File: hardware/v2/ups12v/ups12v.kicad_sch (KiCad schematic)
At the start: 0 parts

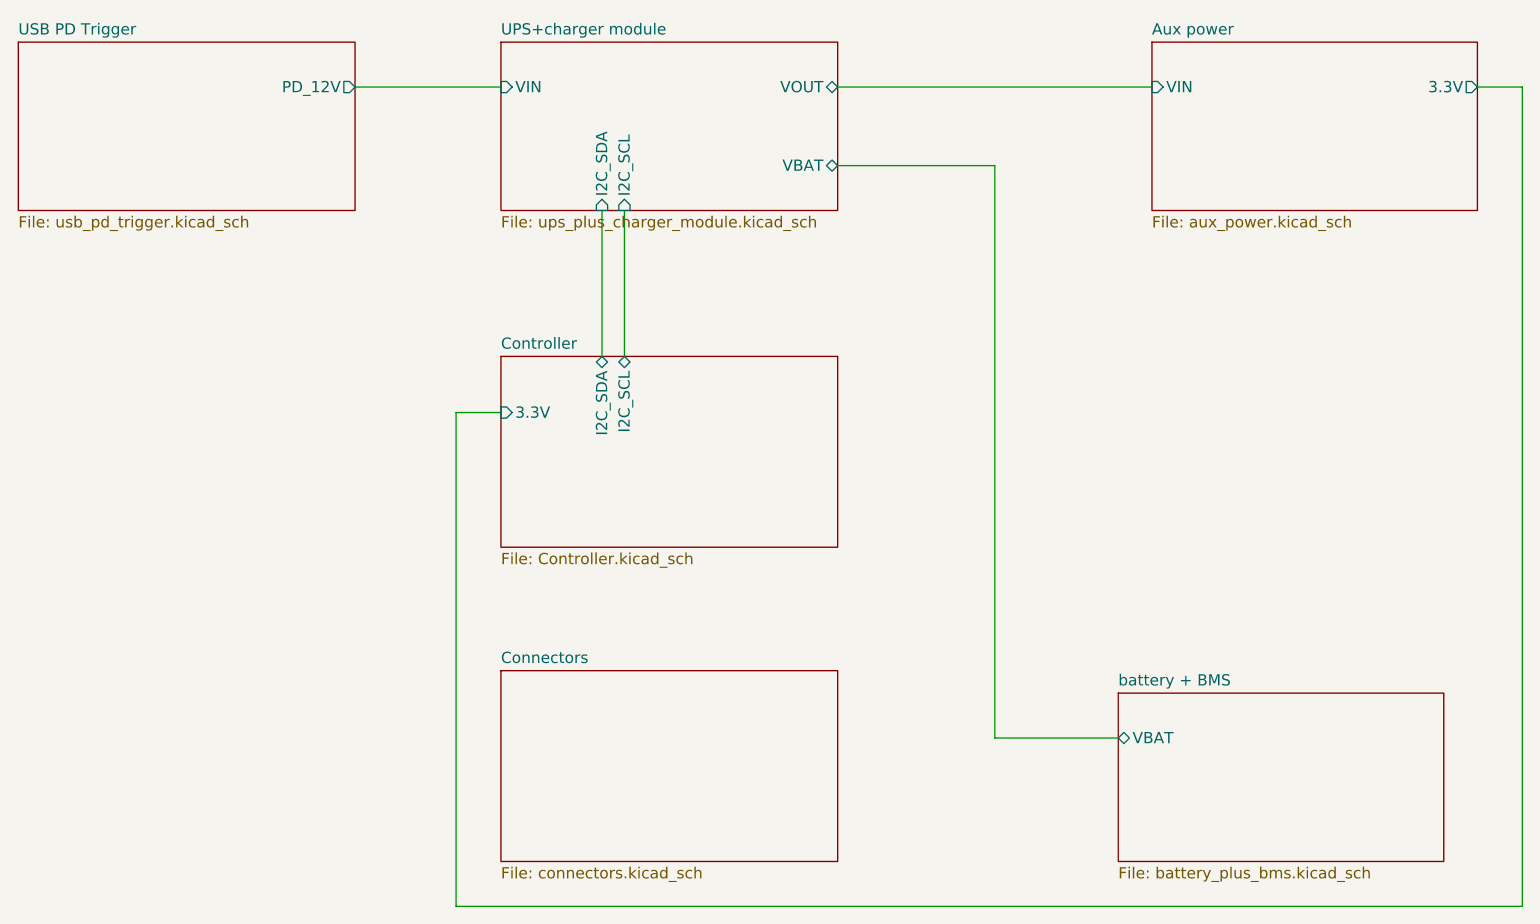
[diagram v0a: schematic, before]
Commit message: add power output to the J4
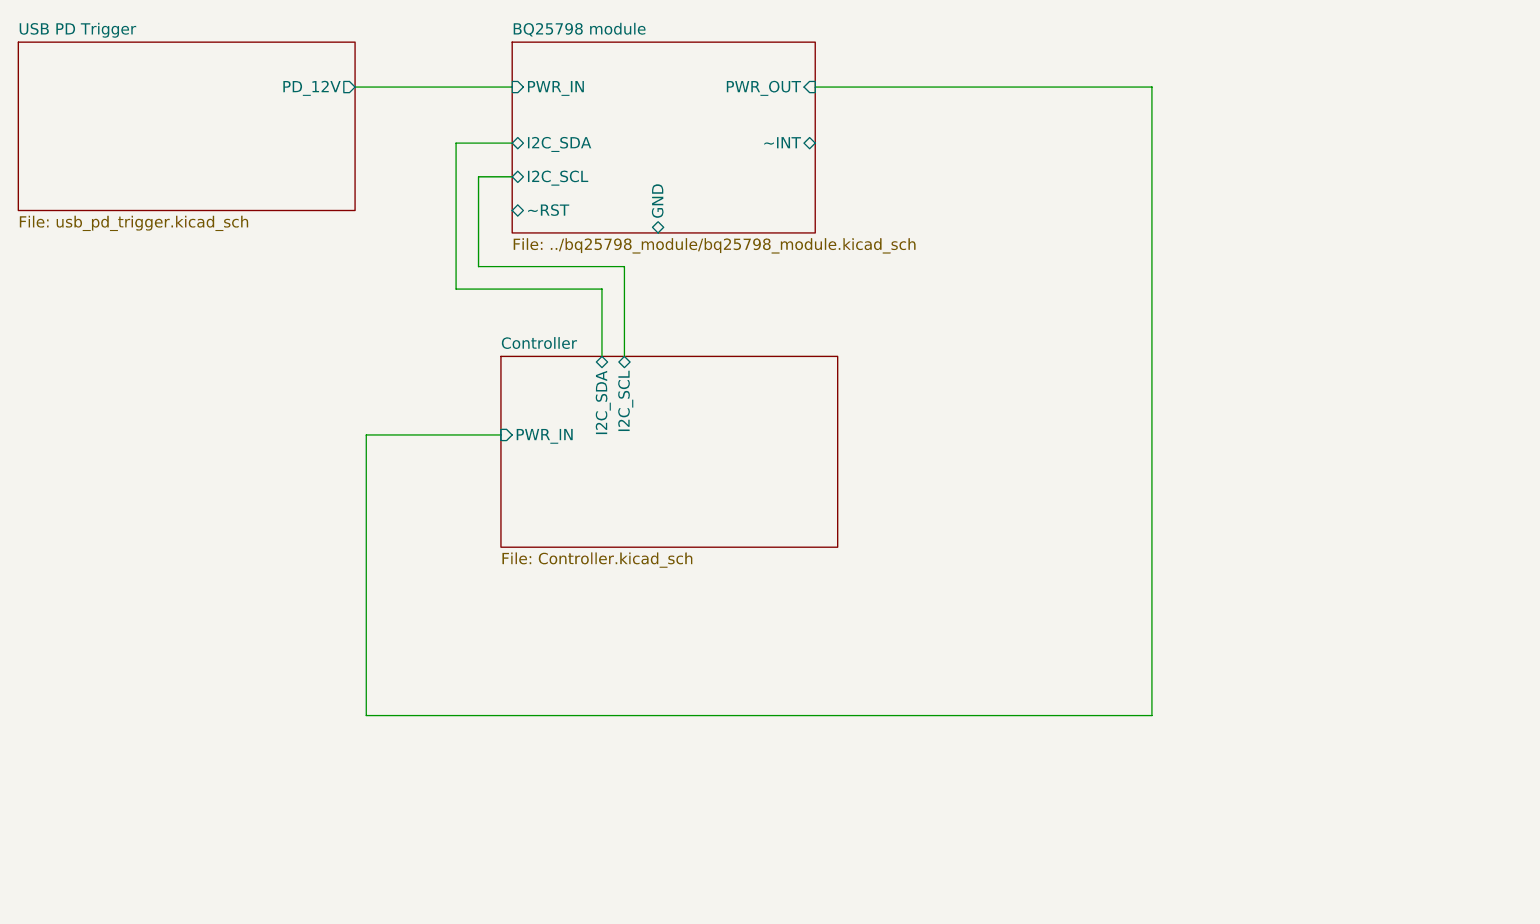
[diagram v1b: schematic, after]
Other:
- removed sheet Aux power
- removed sheet Connectors
- removed sheet UPS+charger module
- removed sheet battery + BMS
- added sheet BQ25798 module (../bq25798_module/bq25798_module.kicad_sch)
- sheet Controller ports: added PWR_IN; removed 3.3V

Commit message: temporary changes to PCB and schematics
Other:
- sheet Controller ports: added GND, ~INT, ~RST; removed none
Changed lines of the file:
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@@
+	(wire
+		(pts
+			(xy 167.64 66.04) (xy 167.64 114.3)
+		)
+		(stroke
+			(width 0)
+			(type default)
+		)
+	)
+	(wire
+		(pts
+			(xy 140.97 68.58) (xy 116.84 68.58)
+		)
+		(stroke
+			(width 0)
+			(type default)
+		)
+	)
 	(wire
 		(pts
@@
 	(wire
 		(pts
+			(xy 118.11 66.04) (xy 167.64 66.04)
+		)
+		(stroke
+			(width 0)
+			(type default)
+		)
+	)
+	(wire
+		(pts
 			(xy 135.89 48.26) (xy 173.99 48.26)
 		)
@@
 	(wire
 		(pts
+			(xy 140.97 54.61) (xy 140.97 68.58)
+		)
+		(stroke
+			(width 0)
+			(type default)
+		)
+	)
+	(wire
+		(pts
+			(xy 119.38 78.74) (xy 119.38 73.66)
+		)
+		(stroke
+			(width 0)
+			(type default)
+		)
+	)
+	(wire
+		(pts
 			(xy 101.6 58.42) (xy 97.79 58.42)
 		)
@@
 	(wire
 		(pts
+			(xy 92.71 73.66) (xy 92.71 62.23)
+		)
+		(stroke
+			(width 0)
+			(type default)
+		)
+	)
+	(wire
+		(pts
 			(xy 111.76 71.12) (xy 111.76 78.74)
 		)
@@
 	(wire
 		(pts
+			(xy 116.84 68.58) (xy 116.84 78.74)
+		)
+		(stroke
+			(width 0)
+			(type default)
+		)
+	)
+	(wire
+		(pts
+			(xy 118.11 64.77) (xy 118.11 66.04)
+		)
+		(stroke
+			(width 0)
+			(type default)
+		)
+	)
+	(wire
+		(pts
+			(xy 119.38 73.66) (xy 92.71 73.66)
+		)
+		(stroke
+			(width 0)
+			(type default)
+		)
+	)
+	(wire
+		(pts
+			(xy 135.89 54.61) (xy 140.97 54.61)
+		)
+		(stroke
+			(width 0)
+			(type default)
+		)
+	)
+	(wire
+		(pts
+			(xy 167.64 114.3) (xy 118.11 114.3)
+		)
+		(stroke
+			(width 0)
+			(type default)
+		)
+	)
+	(wire
+		(pts
+			(xy 118.11 114.3) (xy 118.11 100.33)
+		)
+		(stroke
+			(width 0)
+			(type default)
+		)
+	)
+	(wire
+		(pts
 			(xy 173.99 48.26) (xy 173.99 119.38)
 		)
@@
 		(pts
 			(xy 114.3 68.58) (xy 114.3 78.74)
+		)
+		(stroke
+			(width 0)
+			(type default)
+		)
+	)
+	(wire
+		(pts
+			(xy 92.71 62.23) (xy 101.6 62.23)
 		)
 		(stroke
@@
 			)
 		)
-		(pin "I2C_SCL" bidirectional
+		(pin "I2C_SCL" input
 			(at 101.6 58.42 180)
 			(effects
@@
 			)
 		)
-		(pin "~RST" bidirectional
+		(pin "~RST" input
 			(at 101.6 62.23 180)
 			(effects
@@
 			)
 		)
-		(pin "~INT" bidirectional
+		(pin "~INT" output
 			(at 135.89 54.61 0)
 			(effects
@@
 			)
 		)
-		(pin "I2C_SCL" bidirectional
+		(pin "I2C_SCL" output
 			(at 114.3 78.74 90)
 			(effects
@@
 			)
 		)
+		(pin "~INT" input
+			(at 116.84 78.74 90)
+			(effects
+				(font
+					(size 1.27 1.27)
+				)
+				(justify right)
+			)
+		)
+		(pin "GND" bidirectional
+			(at 118.11 100.33 270)
+			(effects
+				(font
+					(size 1.27 1.27)
+				)
+				(justify left)
+			)
+		)
+		(pin "~RST" output
+			(at 119.38 78.74 90)
+			(effects
+				(font
+					(size 1.27 1.27)
+				)
+				(justify right)
+			)
+		)
